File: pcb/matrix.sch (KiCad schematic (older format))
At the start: 281 parts

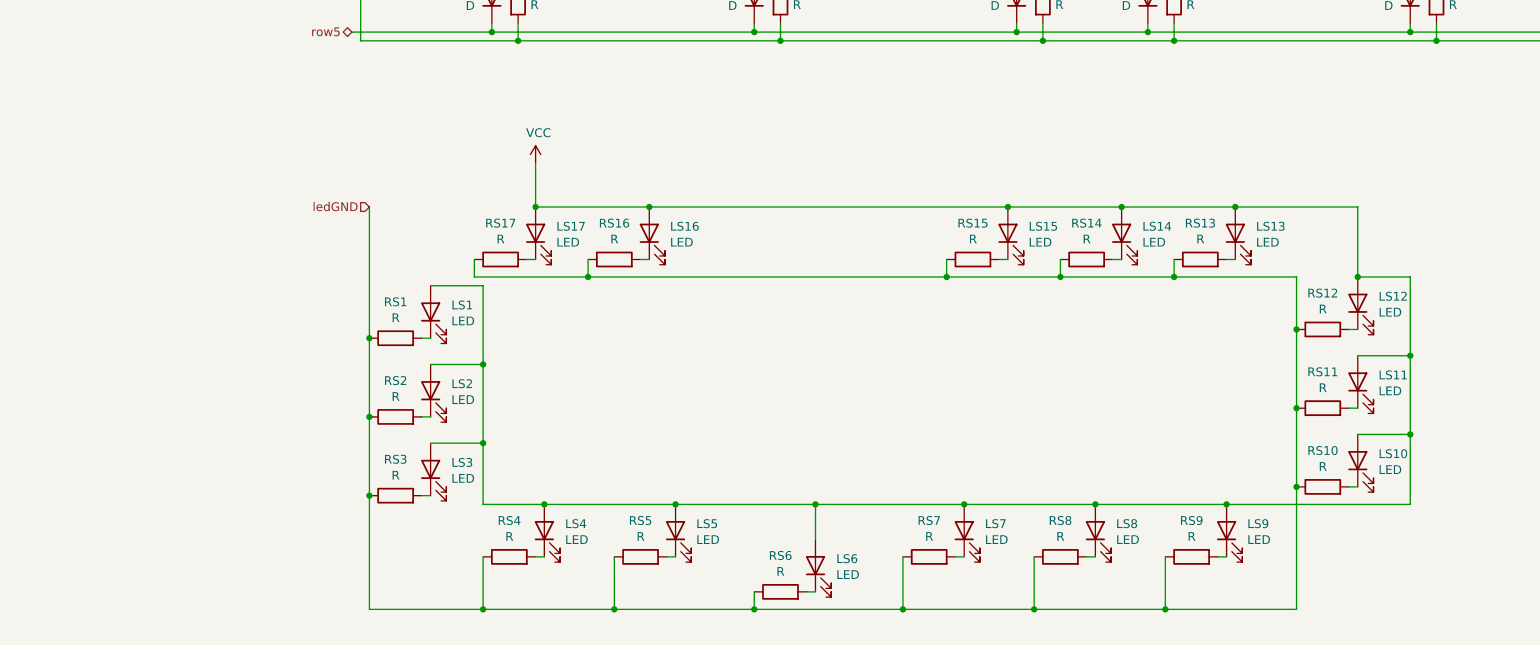
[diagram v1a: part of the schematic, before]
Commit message: Replace single colour underglow and RGB headers for WS2812B Addressable SMD LED
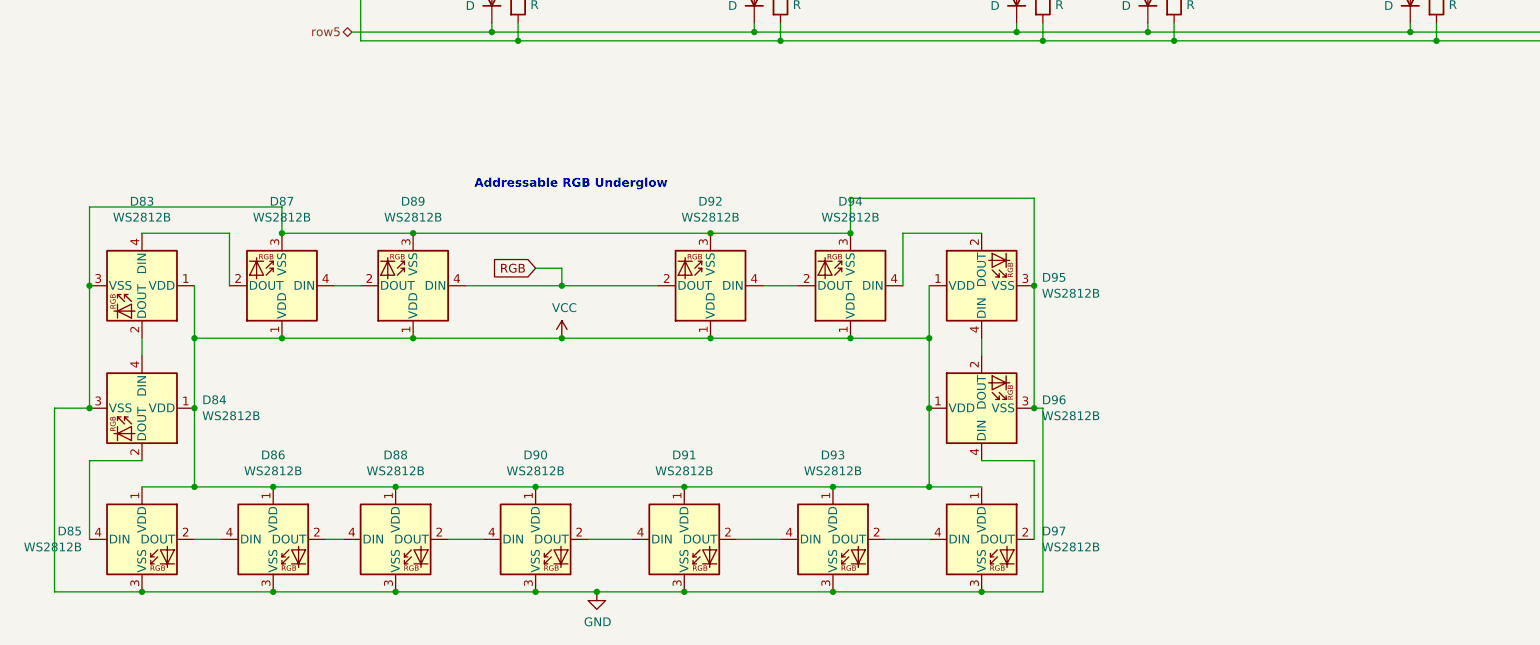
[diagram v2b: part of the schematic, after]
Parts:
- removed LS1, LS10, LS11, LS12, LS13, LS14, LS15, LS16, LS17, LS2, LS3, LS4, LS5, LS6, LS7, LS8, LS9: LED, LED_SMD:LED_0805_2012Metric_Pad1.15x1.40mm_HandSolder, symbol Device:LED
- removed RS1, RS10, RS11, RS12, RS13, RS14, RS15, RS16, RS17, RS2, RS3, RS4, RS5, RS6, RS7, RS8, RS9: R, Resistor_SMD:R_0805_2012Metric_Pad1.15x1.40mm_HandSolder, symbol Device:R
- added D83, D84, D85, D86, D87, D88, D89, D90, D91, D92, D93, D94, D95, D96, D97: WS2812B, LED_SMD:LED_WS2812B_PLCC4_5.0x5.0mm_P3.2mm, symbol LED:WS2812B
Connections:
- net VCC: now also D83.1 (VDD), D84.1 (VDD), D85.1 (VDD), D86.1 (VDD), D87.1 (VDD), D88.1 (VDD), D89.1 (VDD), D90.1 (VDD), D91.1 (VDD), D92.1 (VDD), D93.1 (VDD), D94.1 (VDD), D95.1 (VDD), D96.1 (VDD), D97.1 (VDD)
- new net: D83.2 (DOUT), D84.4 (DIN)
- new net: D83.4 (DIN), D87.2 (DOUT)
- new net: D84.2 (DOUT), D85.4 (DIN)
- new net: D85.2 (DOUT), D86.4 (DIN)
- new net: D94.4 (DIN), D95.2 (DOUT)
- new net: D95.4 (DIN), D96.2 (DOUT)
- new net: D96.4 (DIN), D97.2 (DOUT)
- new net: D93.2 (DOUT), D97.4 (DIN)
- new net: D88.2 (DOUT), D90.4 (DIN)
- new net: D86.2 (DOUT), D88.4 (DIN)
- new net: D90.2 (DOUT), D91.4 (DIN)
- new net: D91.2 (DOUT), D93.4 (DIN)
- new net: D87.4 (DIN), D89.2 (DOUT)
- new net: D92.4 (DIN), D94.2 (DOUT)
- new net GND: D83.3 (VSS), D84.3 (VSS), D85.3 (VSS), D86.3 (VSS), D87.3 (VSS), D88.3 (VSS), D89.3 (VSS), D90.3 (VSS), D91.3 (VSS), D92.3 (VSS), D93.3 (VSS), D94.3 (VSS), D95.3 (VSS), D96.3 (VSS), D97.3 (VSS)
- new net RGB: D89.4 (DIN), D92.2 (DOUT)
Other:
- note added: "Addressable RGB Underglow"

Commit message: Update all components with JLCPCB part numbers
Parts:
- D1, D10, D11, D12, D13, D14, D15, D16, D17, D18, D19, D2, D20, D21, D22, D23, D24, D25, D26, D27, D28, D29, D3, D30, D31, D32, D33, D34, D35, D36, D37, D38, D39, D4, D40, D41, D42, D43, D44, D45, D46, D47, D48, D49, D5, D50, D51, D52, D53, D54, D55, D56, D57, D58, D59, D6, D60, D61, D62, D63, D64, D65, D66, D67, D68, D69, D7, D70, D71, D72, D73, D74, D75, D76, D77, D78, D79, D8, D80, D81, D82, D9: LCSC (none) -> C241939
- D83, D84, D85, D86, D87, D88, D89, D90, D91, D92, D93, D94, D95, D96, D97: LCSC (none) -> C114586
- RL1, RL10, RL11, RL12, RL13, RL14, RL15, RL16, RL17, RL18, RL19, RL2, RL20, RL21, RL22, RL23, RL24, RL25, RL26, RL27, RL28, RL29, RL3, RL30, RL31, RL32, RL33, RL34, RL35, RL36, RL37, RL38, RL39, RL4, RL40, RL41, RL42, RL43, RL44, RL45, RL46, RL47, RL48, RL49, RL5, RL50, RL51, RL52, RL53, RL54, RL55, RL56, RL57, RL58, RL59, RL6, RL60, RL61, RL62, RL63, RL64, RL65, RL66, RL67, RL68, RL69, RL7, RL70, RL71, RL72, RL73, RL74, RL75, RL76, RL77, RL78, RL79, RL8, RL80, RL81, RL82, RL9: LCSC (none) -> C17798-DNP

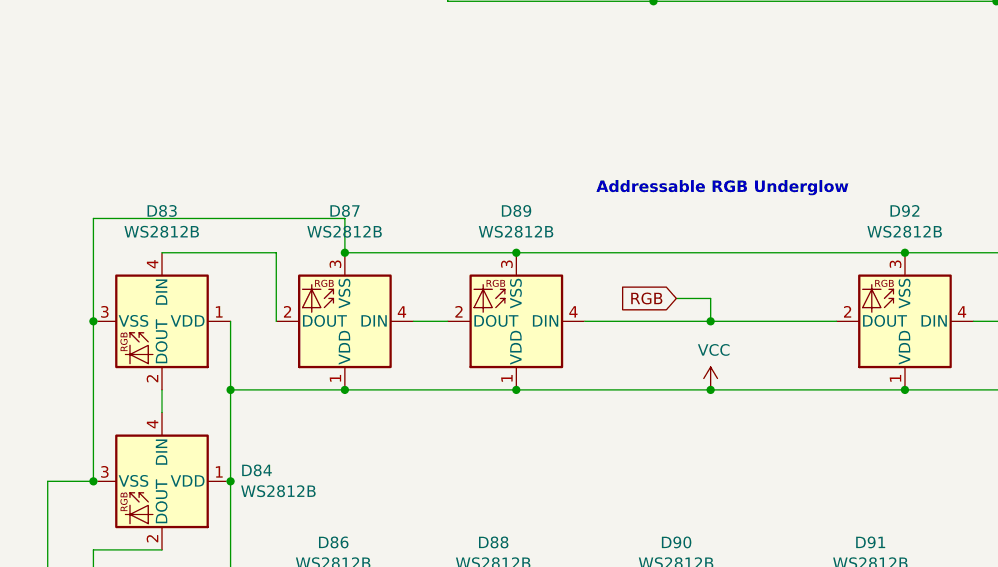
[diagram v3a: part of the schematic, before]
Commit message: Fixed missing VCC for USB connector and incorrect DIN/DOUT for underground LED's
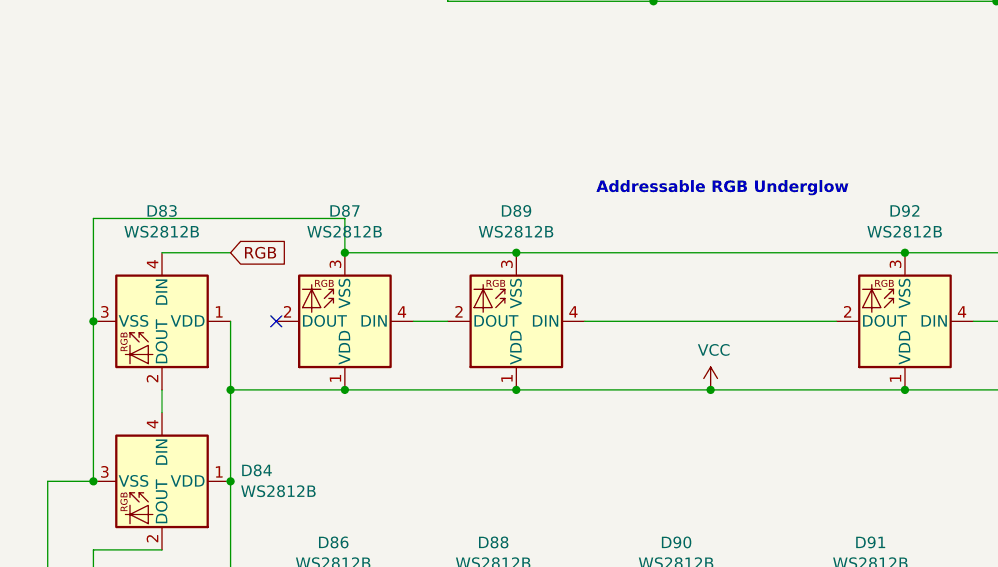
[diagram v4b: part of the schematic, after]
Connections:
- net RGB: now also D83.4 (DIN); no longer D89.4 (DIN), D92.2 (DOUT)
- net at D87.2 (DOUT): no longer D83.4 (DIN)
- new net: D89.4 (DIN), D92.2 (DOUT)
- no-connect marks 0 -> 1

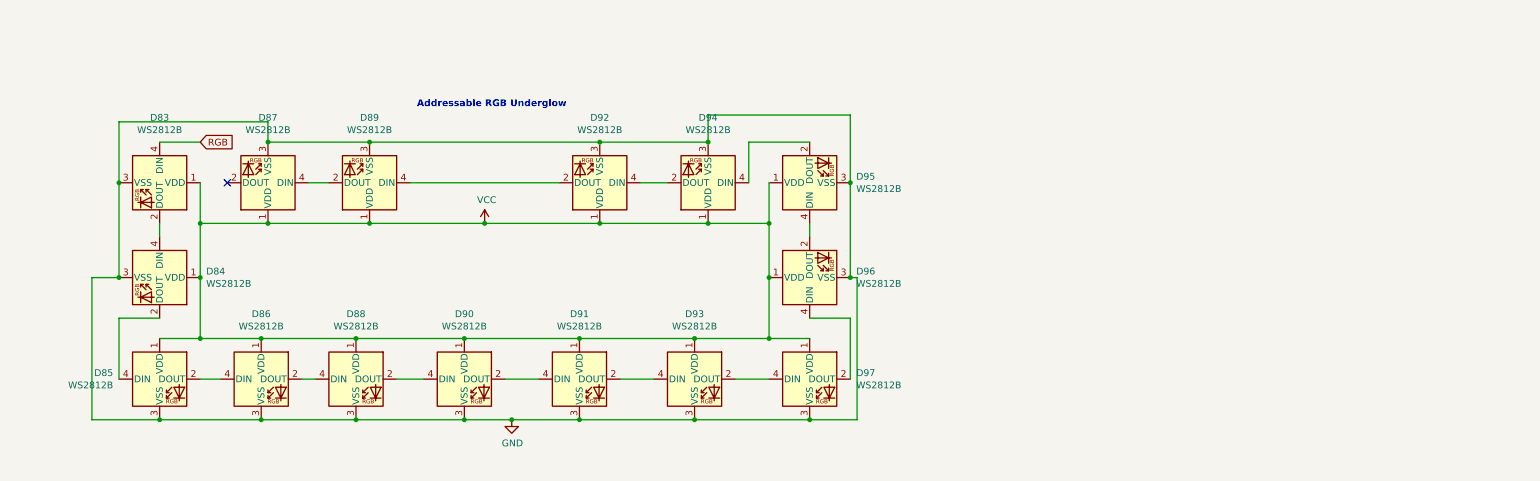
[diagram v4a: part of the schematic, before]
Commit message: Replaced WS21812B with mini version and connected all track. (post clean up commit)
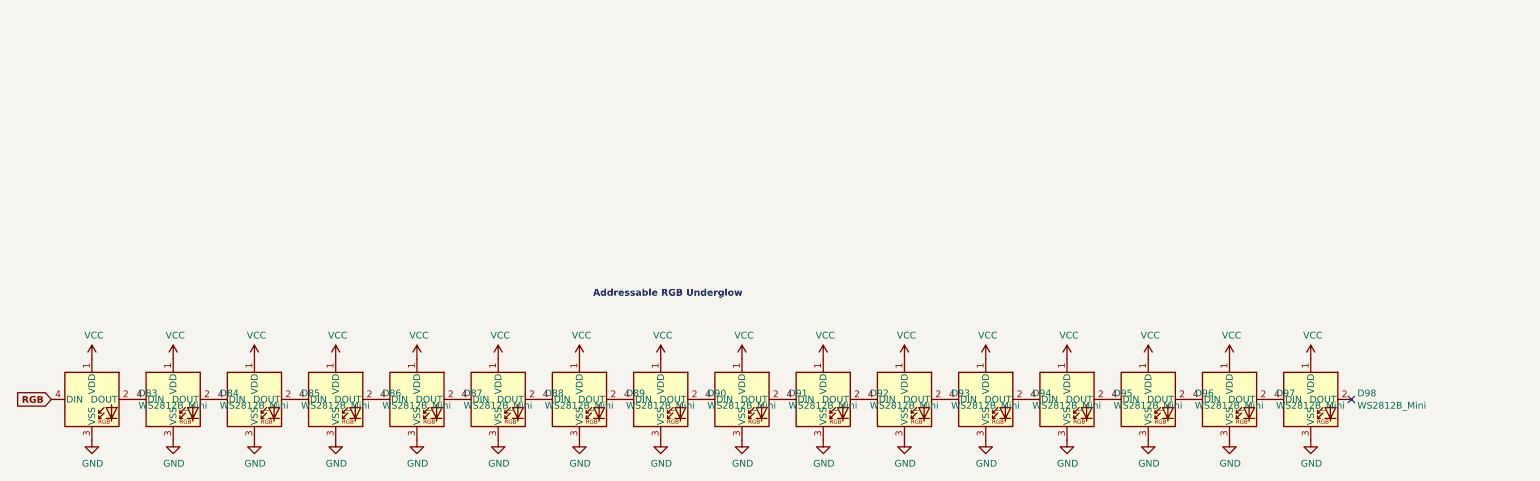
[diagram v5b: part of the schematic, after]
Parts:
- removed D83, D84, D85, D86, D87, D88, D89, D90, D91, D92, D93, D94, D95, D96, D97: WS2812B, LED_SMD:LED_WS2812B_PLCC4_5.0x5.0mm_P3.2mm, symbol LED:WS2812B
- added D83, D84, D85, D86, D87, D88, D89, D90, D91, D92, D93, D94, D95, D96, D97, D98: WS2812B_Mini, LED_SMD:LED_SK6812MINI_PLCC4_3.5x3.5mm_P1.75mm, symbol WS2812B_Mini:WS2812B_Mini
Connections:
- net GND: now also D83.3 (VSS), D84.3 (VSS), D85.3 (VSS), D86.3 (VSS), D87.3 (VSS), D88.3 (VSS), D89.3 (VSS), D90.3 (VSS), D91.3 (VSS), D92.3 (VSS), D93.3 (VSS), D94.3 (VSS), D95.3 (VSS), D96.3 (VSS), D97.3 (VSS), D98.3 (VSS)
- net RGB: now also D83.4 (DIN)
- net VCC: now also D83.1 (VDD), D84.1 (VDD), D85.1 (VDD), D86.1 (VDD), D87.1 (VDD), D88.1 (VDD), D89.1 (VDD), D90.1 (VDD), D91.1 (VDD), D92.1 (VDD), D93.1 (VDD), D94.1 (VDD), D95.1 (VDD), D96.1 (VDD), D97.1 (VDD), D98.1 (VDD)
- new net: D83.2 (DOUT), D84.4 (DIN)
- new net: D84.2 (DOUT), D85.4 (DIN)
- new net: D85.2 (DOUT), D86.4 (DIN)
- new net: D86.2 (DOUT), D87.4 (DIN)
- new net: D87.2 (DOUT), D88.4 (DIN)
- new net: D88.2 (DOUT), D89.4 (DIN)
- new net: D89.2 (DOUT), D90.4 (DIN)
- new net: D90.2 (DOUT), D91.4 (DIN)
- new net: D91.2 (DOUT), D92.4 (DIN)
- new net: D92.2 (DOUT), D93.4 (DIN)
- new net: D93.2 (DOUT), D94.4 (DIN)
- new net: D94.2 (DOUT), D95.4 (DIN)
- new net: D95.2 (DOUT), D96.4 (DIN)
- new net: D96.2 (DOUT), D97.4 (DIN)
- new net: D97.2 (DOUT), D98.4 (DIN)
